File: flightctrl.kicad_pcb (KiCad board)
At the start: 2 copper layers, 150 x 120 mm, 71 parts, among them J1 USB_OTG, J2 CONN_01X02, J3 CONN_01X02, J4 CONN_01X02, J5 CONN_01X02, J6 CONN_01X02, J7 CONN_01X02, J8 BARREL_JACK, P1 CONN_02X03, Q1 2N7000, Q2 2N7000, Q3 2N7000, Q4 2N7000, Q5 2N7000, Q6 Q_PMOS_SGD, Q7 2N7000, SW1 ROTARY_ENCODER_SWITCH, SW2 SW_SPST, SW3 SW_SPST, SW4 SW_SPST, SW5 ROTARY_ENCODER_SWITCH, SW6 SW_SPST, SW7 SW_SPST, SW8 SW_SPST, U1 ATMEGA328P-AU, U2 LM2931AZ-5.0, Y1 12MHz

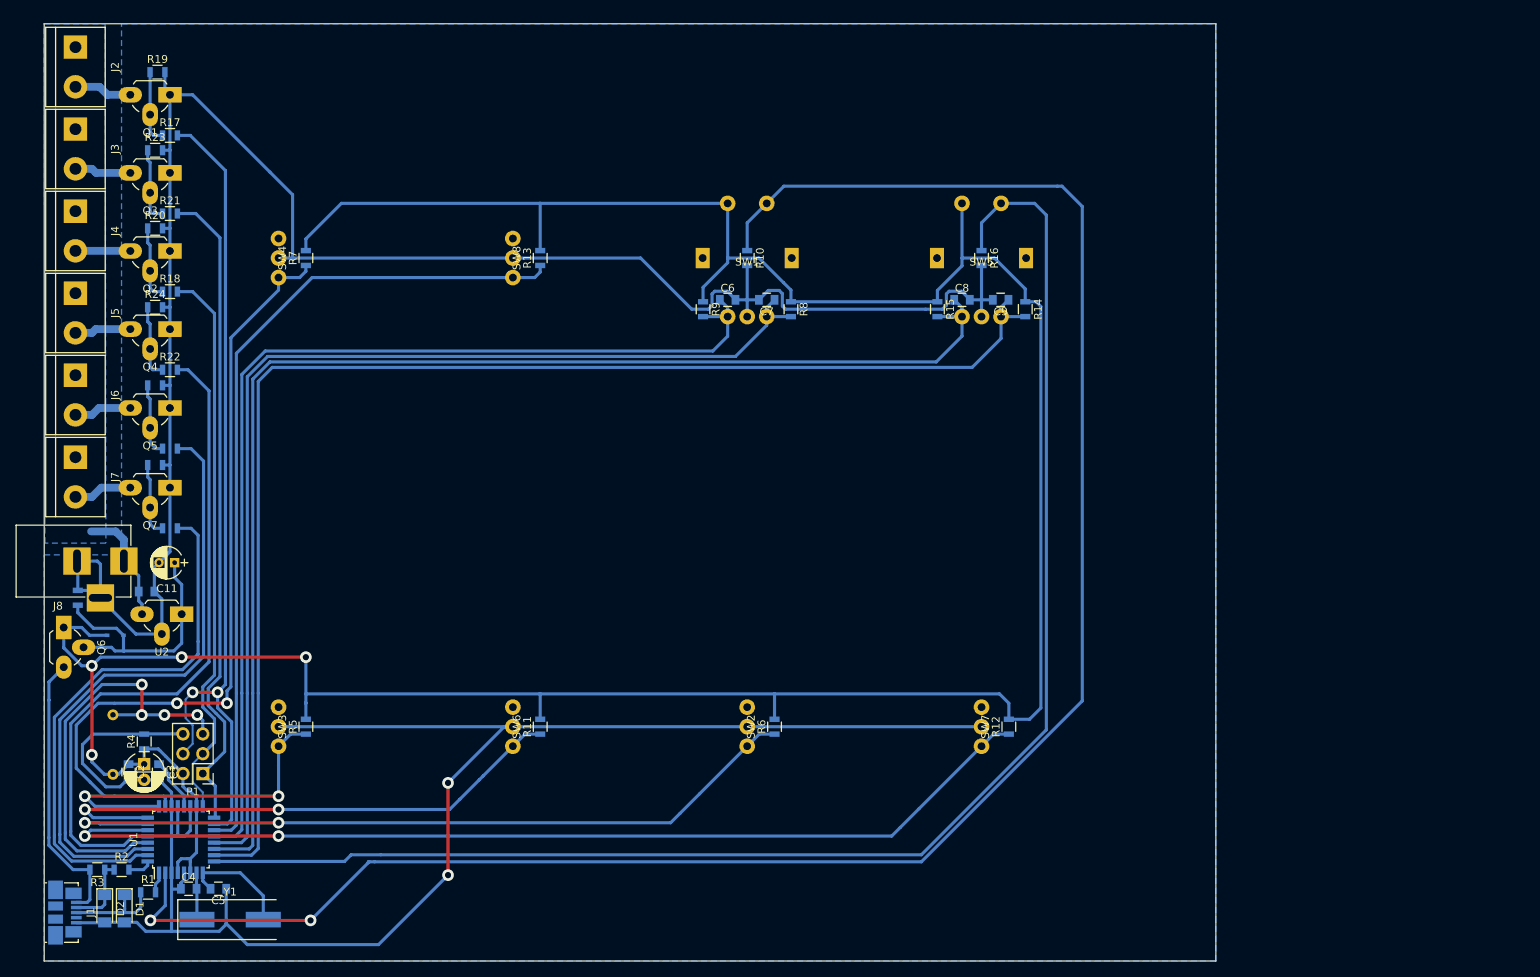
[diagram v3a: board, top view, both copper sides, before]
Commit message: update project for KiCAD 5.0, recreate/fix PCB
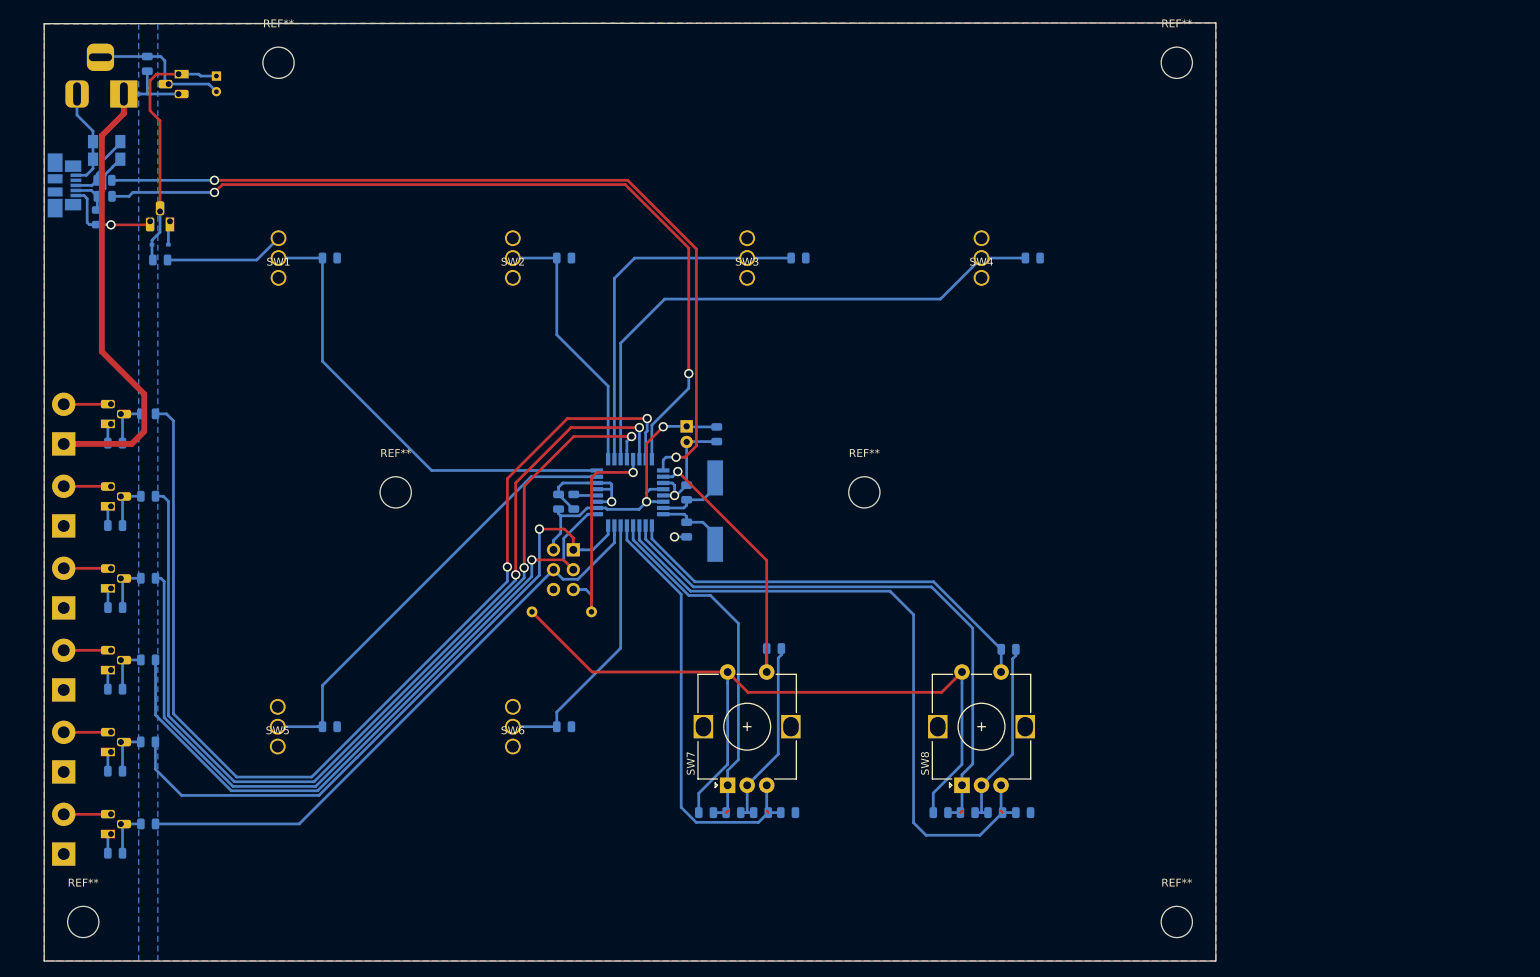
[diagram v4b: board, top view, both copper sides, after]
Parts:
- added G***: LOGO, misc:logo_didee, B.Cu at (176.4, 55.9)
- added REF**: MountingHole_4mm, MountingHole:MountingHole_4mm, F.Cu at (185.0, 155.0)
- added REF**: MountingHole_4mm, MountingHole:MountingHole_4mm, F.Cu at (185.0, 45.0)
- added REF**: MountingHole_4mm, MountingHole:MountingHole_4mm, F.Cu at (45.0, 155.0)
- added REF**: MountingHole_4mm, MountingHole:MountingHole_4mm, F.Cu at (70.0, 45.0)
- added REF**: MountingHole_4mm, MountingHole:MountingHole_4mm, F.Cu at (145.0, 100.0)
- added REF**: MountingHole_4mm, MountingHole:MountingHole_4mm, F.Cu at (85.0, 100.0)
- C1: footprint Capacitors_ThroughHole:CP_Radial_D5.0mm_P2.00mm -> Capacitor_THT:CP_Radial_D5.0mm_P2.00mm; moved to B.Cu
- C10, C2, C3, C4, C5, C6, C7, C8, C9: footprint Capacitors_SMD:C_0805 -> Capacitor_SMD:C_0805_2012Metric
- C11: footprint Capacitors_ThroughHole:CP_Radial_D4.0mm_P2.00mm -> Capacitor_THT:CP_Radial_D4.0mm_P2.00mm; moved to B.Cu
- D1, D2: footprint Diodes_SMD:D_MiniMELF -> Diode_SMD:D_MiniMELF
- D3: footprint Diodes_SMD:D_SOD-323 -> Diode_SMD:D_SOD-323
- J2, J3, J4, J5, J6, J7: footprint Terminal_Blocks:TerminalBlock_bornier-2_P5.08mm -> TerminalBlock:TerminalBlock_bornier-2_P5.08mm
- J8: footprint Connect:BARREL_JACK -> Connector_BarrelJack:BarrelJack_Horizontal; moved to B.Cu
- P1: footprint Pin_Headers:Pin_Header_Straight_2x03_Pitch2.54mm -> Connector_PinHeader_2.54mm:PinHeader_2x03_P2.54mm_Vertical; moved to B.Cu
- Q1, Q2, Q3, Q4, Q5, Q7: footprint TO_SOT_Packages_THT:TO-92_Rugged -> Package_TO_SOT_THT:TO-92_HandSolder
- Q6, U2: footprint TO_SOT_Packages_THT:TO-92_Rugged -> Package_TO_SOT_THT:TO-92_HandSolder; moved to B.Cu
- R1, R10, R11, R12, R13, R14, R15, R16, R17, R18, R19, R2, R20, R21, R22, R23, R24, R25, R26, R27, R29, R3, R30, R4, R5, R6, R7, R8, R9: footprint Resistors_SMD:R_0805 -> Resistor_SMD:R_0805_2012Metric
- R31: footprint Resistors_ThroughHole:R_Axial_DIN0204_L3.6mm_D1.6mm_P7.62mm_Horizontal -> Resistor_THT:R_Axial_DIN0204_L3.6mm_D1.6mm_P7.62mm_Horizontal; moved to B.Cu
- SW1, SW5: value ROTARY_ENCODER_SWITCH -> SW_SPST; footprint Button_Switch_THT:PEC11R-4xxxF-Sxxx -> Button_Switch_THT:MKIP1PUM; moved to F.Cu
- SW2, SW3, SW4, SW6: moved to F.Cu
- SW7, SW8: value SW_SPST -> Rotary_Encoder_Switch; footprint Button_Switch_THT:MKIP1PUM -> Rotary_Encoder:RotaryEncoder_Alps_EC12E-Switch_Vertical_H20mm; moved to F.Cu
- U1: footprint Housings_QFP:TQFP-32_7x7mm_Pitch0.8mm -> Package_QFP:TQFP-32_7x7mm_P0.8mm
- Y1: footprint Crystals:Crystal_SMD_HC49-SD -> Crystal:Crystal_SMD_HC49-SD
- moved SW5 108.2 mm to (69.9, 130.0)
- moved J2 103.3 mm to (42.5, 146.3), turned to 90 degrees
- moved R19 100.1 mm to (49.1, 146.2), turned to 180 degrees
- moved D1 98.2 mm to (48.0, 55.1), turned to 180 degrees
- moved D2 96.0 mm to (48.0, 57.4), turned to 180 degrees
- moved Q1 94.9 mm to (48.5, 143.7), turned to 90 degrees
- moved J1 93.1 mm to (42.6, 60.7), turned to 90 degrees
- moved R1 91.3 mm to (47.7, 60.0)
- moved SW4 90.0 mm to (160.0, 70.0), turned to 0 degrees
- moved SW8 88.7 mm to (157.5, 137.5)
- moved R17 88.2 mm to (53.3, 142.4)
- moved R2 86.2 mm to (47.7, 62.1)
- moved SW3 84.9 mm to (130.0, 70.0), turned to 0 degrees
- moved R3 83.5 mm to (46.8, 64.8), turned to 270 degrees
- moved R4 83.2 mm to (126.1, 92.6), turned to 270 degrees
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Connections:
- SW1 pad 1: SW7_A -> SW1
- SW1 pad 3: SW7_B -> (no net)
- SW2 pad 1: SW3 -> SW2
- SW3 pad 1: SW1 -> SW3
- SW4 pad 1: SW5 -> SW4
- SW5 pad 1: SW8_A -> SW5
- SW5 pad 3: SW8_B -> (no net)
- SW6 pad 1: SW2 -> SW6
- U1 pad 10: SW8_B -> SW8_A
- U1 pad 11: SW8_A -> SW8_B
- U1 pad 12: SW7_B -> SW7_A
- U1 pad 13: SW7_A -> SW7_B
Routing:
- net GND: track 478.8 -> 146.7 mm, vias 2 -> 3
- net +5V: track 384.9 -> 143.1 mm, vias 4 -> 2
- net SW7_C: track 250.9 -> 35.5 mm, vias 2 -> 1
- net SW8_C: track 192.9 -> 55.2 mm
- net USB_DP: track 2.69 -> 110.0 mm, vias 0 -> 2
- net USB_DM: track 3.13 -> 106.8 mm, vias 0 -> 2
- net SW8_A: track 166.1 -> 73.9 mm
- net SW7_A: track 134.6 -> 46.0 mm
- net SW8_B: track 171.6 -> 85.8 mm
- net SW7_B: track 139.5 -> 56.3 mm
- net SW6: track 107.6 -> 34.8 mm
- net OUT6: track 69.3 -> 136.2 mm, vias 0 -> 2
- net SW4: track 132.1 -> 71.2 mm, vias 2 -> 0
- net +12V: track 15.1 -> 69.7 mm
- net SW3: track 101.1 -> 46.9 mm, vias 2 -> 0
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- added copper zone on B.Cu, net +5V
- added copper zone on F.Cu, net GND
- removed copper zone on B.Cu, net GND
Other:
- board size 150 x 120 mm -> 150 x 120.1 mm
- net class Default: via_dia 0.6 -> 0.8
